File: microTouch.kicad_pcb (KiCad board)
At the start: 2 copper layers, 34.5 x 22.9 mm, 10 parts, among them J1 SERVO, J2 PRINTER, U1 A3144

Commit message: a few more layout tweaks
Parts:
- U1: footprint Package_TO_SOT_THT:TO-92Flat -> microTouch:TO-92Flat_Oval
- moved J2 1.06 mm to (99.1, 88.9)
- moved D1 0.56 mm to (111.3, 89.9)
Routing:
- net /SERVO: track 20.2 -> 21.0 mm, vias 2 -> 1
- net /SIG: track 18.2 -> 19.1 mm
- net Net-(D1-Pad1): track 12.9 -> 13.7 mm
- net /5V: track 50.5 -> 50.3 mm, vias 3 -> 2
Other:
- rule pad_to_mask_clearance: 0 -> 0.05

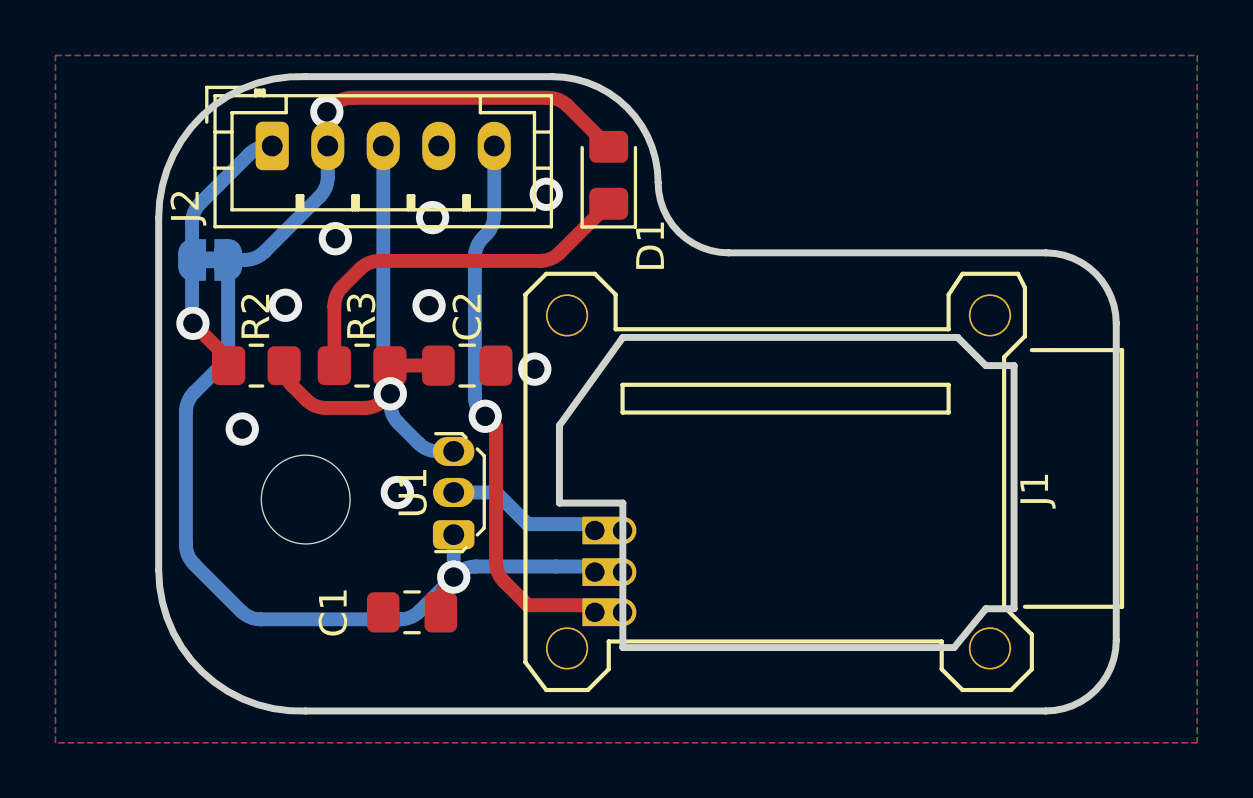
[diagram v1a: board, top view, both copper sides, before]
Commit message: redo the track rounding
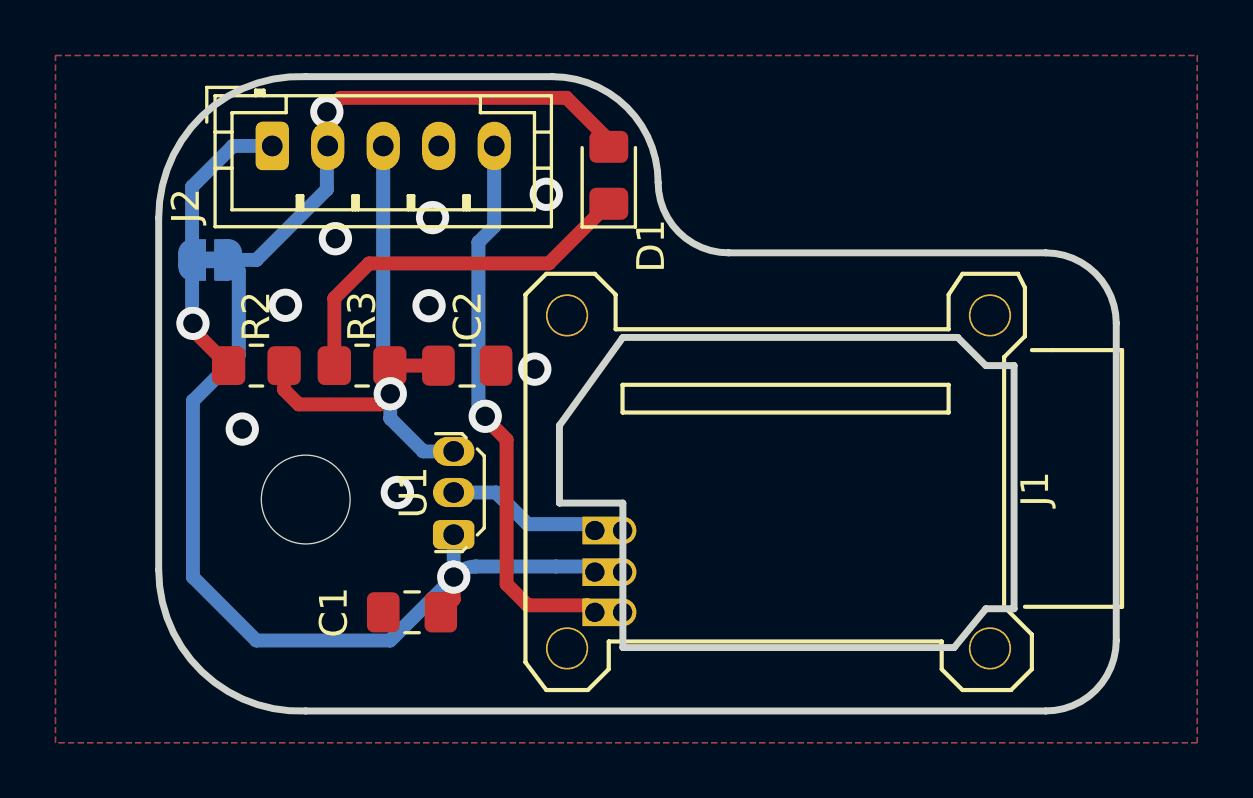
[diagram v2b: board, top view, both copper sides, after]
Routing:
- net /5V: track 50.3 -> 51.9 mm
- net /SERVO: track 21.0 -> 20.2 mm
- net /VSIG: track 9.87 -> 10.5 mm

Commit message: forgot to label the bins in the silk screen
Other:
- board text added: "5V"
- board text added: "GND"
- board text added: "SERVO"
- board text added: "SIG"
- board text added: "VSIG"
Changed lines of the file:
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@@
     (effects (font (size 1 1) (thickness 0.2)) (justify mirror))
+  )
+  (gr_text "VSIG" (at 99.06 89.916 90) (layer "B.SilkS")
+    (effects (font (size 1 1) (thickness 0.15)) (justify left mirror))
+  )
+  (gr_text "SIG" (at 103.124 89.916 90) (layer "B.SilkS")
+    (effects (font (size 1 1) (thickness 0.15)) (justify left mirror))
+  )
+  (gr_text "GND" (at 105.156 89.916 90) (layer "B.SilkS")
+    (effects (font (size 1 1) (thickness 0.15)) (justify left mirror))
+  )
+  (gr_text "5V" (at 101.092 89.916 90) (layer "B.SilkS")
+    (effects (font (size 1 1) (thickness 0.15)) (justify left mirror))
   )
   (gr_text "microTouch v1.1" (at 117.348 108.077) (layer "B.SilkS")
     (effects (font (size 1 1) (thickness 0.2)) (justify mirror))
   )
+  (gr_text "SERVO" (at 107.188 89.916 90) (layer "B.SilkS")
+    (effects (font (size 1 1) (thickness 0.15)) (justify left mirror))
+  )
   (segment (start 109.093 93.091) (end 102.616 93.091) (width 0.5) (layer "F.Cu") (net 1))
